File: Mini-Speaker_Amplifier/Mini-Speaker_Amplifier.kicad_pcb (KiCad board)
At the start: 2 copper layers, 30 x 48 mm, 20 parts, among them J1 AudioJack2, J2 Conn_02x05, J3 Conn_01x02, U1 LM386-4

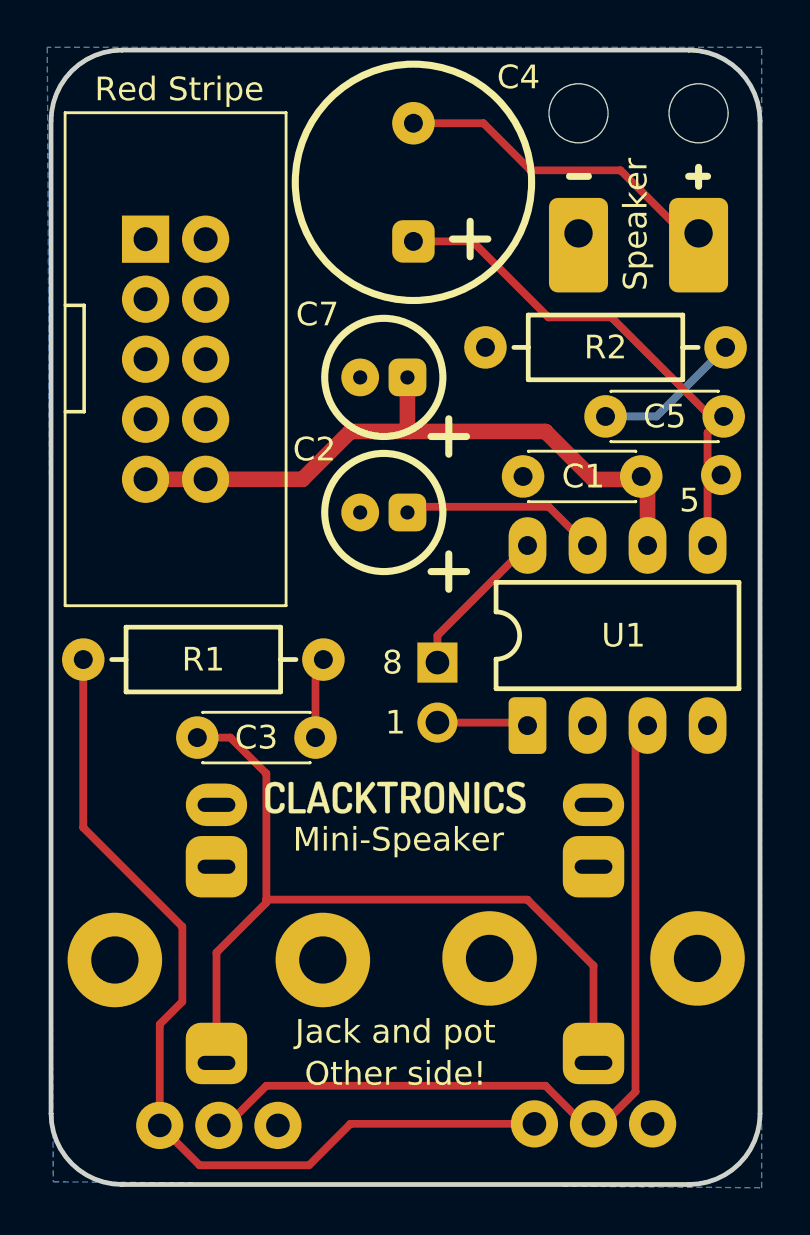
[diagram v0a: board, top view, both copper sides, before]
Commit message: Added reverse protection diode Make grid raster 0.5080
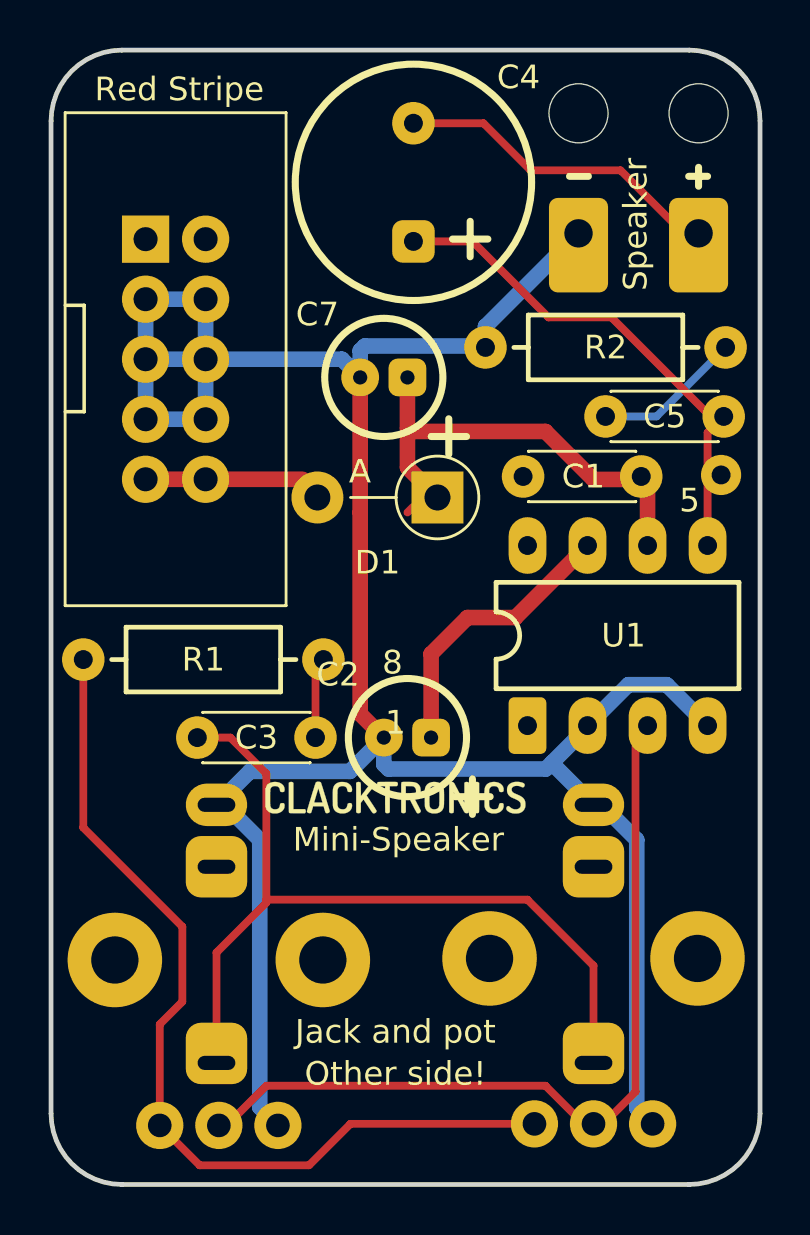
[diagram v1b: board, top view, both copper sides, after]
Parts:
- removed J3: Conn_01x02, Connector_PinHeader_2.54mm:PinHeader_1x02_P2.54mm_Vertical
- added D1: 1N5817, Diode_THT:D_DO-41_SOD81_P5.08mm_Vertical_AnodeUp, F.Cu at (133.3, 74.9)
- R1: value 470k -> 470kΩ
- R2: value 10 -> 10Ω
- RV1 (x2): value 10k -> 10kΩ
- U1: value LM386-4 -> LM386
- moved C2 9.58 mm to (132.1, 85.1)
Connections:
- J2 pad 1: (no net) -> Net-(J2-Pad1)
- J2 pad 10: +12V -> Net-(D1-Pad2)
- J2 pad 2: (no net) -> Net-(J2-Pad2)
- J2 pad 9: +12V -> Net-(D1-Pad2)
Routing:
- net GND: track 0.13 -> 110.9 mm
- net Net-(D1-Pad2): track 0.00 -> 6.64 mm
- net Net-(U1-Pad8): track 6.53 -> 0.00 mm
- net +12V: track 28.0 -> 22.7 mm
- net Net-(U1-Pad1): track 3.86 -> 0.18 mm
- net Net-(C2-Pad1): track 8.40 -> 12.1 mm
- removed copper zone on B.Cu, net GND
